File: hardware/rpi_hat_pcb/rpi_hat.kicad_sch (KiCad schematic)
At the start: 6 parts, among them J1 GPIO, U1 CAT24C256

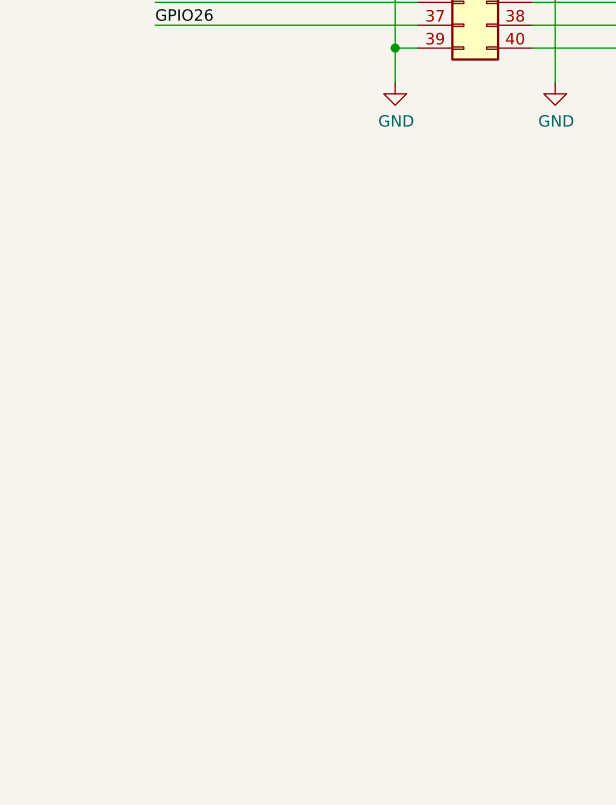
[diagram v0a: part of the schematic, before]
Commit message: Update the pcb layout and spice simulation
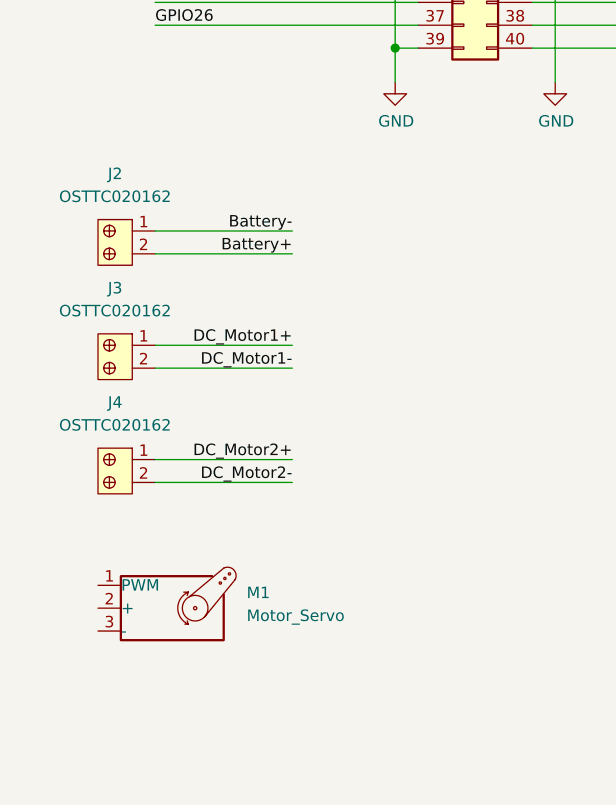
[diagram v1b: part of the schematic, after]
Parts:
- added J2, J3, J4: OSTTC020162, digikey-footprints:Term_Block_1x2_P5mm, symbol dk_Terminal-Blocks-Wire-to-Board:OSTTC020162
- added M1: Motor_Servo, Connector_PinHeader_2.54mm:PinHeader_1x03_P2.54mm_Vertical, symbol Motor:Motor_Servo
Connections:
- new net Battery+: J2.2
- new net Battery-: J2.1
- new net DC_Motor1+: J3.1
- new net DC_Motor1-: J3.2
- new net DC_Motor2+: J4.1
- new net DC_Motor2-: J4.2

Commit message: Update the connectors for the board
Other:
- note removed: "Additional pin functions: https://pinout.xyz/"
- company: (none) -> RIT MSD Team 18538
- title: (none) -> Raspberrypi Motor and power Hat
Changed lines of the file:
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@@
   (paper "A4")
   (title_block
-    (date "15 nov 2012")
+    (title "Raspberrypi Motor and power Hat")
+    (date "2023-11-15")
+    (rev "V0.0.1")
+    (company "RIT MSD Team 18538")
   )
   (junction (at 93.98 175.26) (diameter 1.016) (color 0 0 0 0)
@@
     (stroke (width 0) (type solid))
   )
-  (text "Additional pin functions:\nhttps://pinout.xyz/" (at 179.07 180.34 0)
-    (effects (font (size 1.27 1.27)) (justify left bottom))
-  )
   (text "ID_SD and ID_SC PINS:\nThese pins are reserved for HAT ID EEPROM.\n\nAt boot time this I2C interface will be\ninterrogated to look for an EEPROM\nthat identifes the attached board and\nallows automagic setup of the GPIOs\n(and optionally, Linux drivers).\n\nBridging JP1 enables write protection.\n\nDO NOT USE these pins for anything other\nthan attaching an I2C ID EEPROM. Leave\nunconnected if ID EEPROM not required."
